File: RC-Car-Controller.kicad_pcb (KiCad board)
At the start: 2 copper layers, 72 parts, among them J1 USB_C_Receptacle_USB2.0, J2 Power_Input, J3 Screw_Terminal_01x02, J4 Motor_1_input, J5 Motor_2_input, SW1 SW_Push, SW2 SW_Push, U1 W25Q32JVSS, U2 ESP32-C3, U3 USBLC6-2SC6, U4 LMR14020SDDAR, U6 BMI055, U7 SPX3819M5-L-3-3, U8 DRV8874PWPR, U9 DRV8874PWPR, X1 40MHz

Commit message: Update placement
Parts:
- removed J3: Screw_Terminal_01x02, TerminalBlock:TerminalBlock_bornier-2_P5.08mm
- removed R11, R5, R6: 5k1, Resistor_SMD:R_0603_1608Metric
- removed R7: 1k, Resistor_SMD:R_0603_1608Metric
- removed R9: 10K, Resistor_SMD:R_0603_1608Metric
- removed SW1: SW_Push, Button_Switch_SMD:SW_Push_SPST_NO_Alps_SKRK
- removed X1: 40MHz, Crystal:Crystal_SMD_2520-4Pin_2.5x2.0mm
- added C34: 1uF, Capacitor_SMD:C_0402_1005Metric, F.Cu at (62.9, 35.9)
- added C35: 100n, Capacitor_SMD:C_0402_1005Metric, F.Cu at (37.4, 81.8)
- added C36: 22n, Capacitor_SMD:C_0402_1005Metric, F.Cu at (70.1, 51.9)
- added C37: 100n, Capacitor_SMD:C_0402_1005Metric, F.Cu at (71.9, 51.9)
- added C38: 100n, Capacitor_SMD:C_0402_1005Metric, F.Cu at (72.9, 50.8)
- added C39: 100u, Capacitor_SMD:C_0805_2012Metric, F.Cu at (73.6, 49.3)
- added C40: 100n, Capacitor_SMD:C_0402_1005Metric, F.Cu at (71.9, 68.9)
- added C41: 22n, Capacitor_SMD:C_0402_1005Metric, F.Cu at (69.9, 68.9)
- added C42: 100n, Capacitor_SMD:C_0402_1005Metric, F.Cu at (73.0, 67.9)
- added C43: 100u, Capacitor_SMD:C_0805_2012Metric, F.Cu at (73.7, 66.4)
- added C44: 100u, Capacitor_SMD:C_0805_2012Metric, F.Cu at (36.6, 83.3)
- added J6: MOTOR_3_OUTPUT, TerminalBlock:TerminalBlock_bornier-2_P5.08mm, F.Cu at (27.4, 54.9)
- added J7: MOTOR_4_OUTPUT, TerminalBlock:TerminalBlock_bornier-2_P5.08mm, F.Cu at (27.4, 71.4)
- added R14: 10K, Resistor_SMD:R_0603_1608Metric, F.Cu at (56.1, 68.9)
- added R15: 10K, Resistor_SMD:R_0603_1608Metric, F.Cu at (56.1, 65.7)
- added SW4: SW_Push, Button_Switch_SMD:SW_Push_SPST_NO_Alps_SKRK, F.Cu at (60.2, 81.6)
- added U10: DRV8874PWPR, Libraries:SOP65P640X120-17N, F.Cu at (71.5, 74.3)
- added U11: DRV8874PWPR, Libraries:SOP65P640X120-17N, F.Cu at (38.8, 74.7)
- added X2: 40MHz, KiCADv7:OSC_X322516MLB4SI, F.Cu at (66.2, 39.1)
- C1: value 100n -> 4.7u/100v; footprint Capacitor_SMD:C_0603_1608Metric -> Capacitor_SMD:C_1812_4532Metric
- C10, C9: value 10p -> 100n
- C11: value 100n -> 22n; footprint Capacitor_SMD:C_0603_1608Metric -> Capacitor_SMD:C_0402_1005Metric
- C12, C18, C20, C21, C22, C3, C30, C32, C4, C7: footprint Capacitor_SMD:C_0603_1608Metric -> Capacitor_SMD:C_0402_1005Metric
- C13, C24: value 10u -> 100n; footprint Capacitor_SMD:C_0603_1608Metric -> Capacitor_SMD:C_0402_1005Metric
- C14: value 4.7u/100v -> 100u; footprint Capacitor_SMD:C_1812_4532Metric -> Capacitor_SMD:C_0805_2012Metric
- C15: value 100n/100v -> 100n; footprint Capacitor_SMD:C_0805_2012Metric -> Capacitor_SMD:C_0402_1005Metric
- C16: value 0.1u -> 100n; footprint Capacitor_SMD:C_0603_1608Metric -> Capacitor_SMD:C_0402_1005Metric
- C17: value 10u -> 22n; footprint Capacitor_SMD:C_0603_1608Metric -> Capacitor_SMD:C_0402_1005Metric
- C19, C27, C6: value 100n -> 10u
- C2: value 10u -> 100n/100v; footprint Capacitor_SMD:C_1210_3225Metric -> Capacitor_SMD:C_0805_2012Metric
- C23: value 100n -> 20p; footprint Capacitor_SMD:C_0603_1608Metric -> Capacitor_SMD:C_0402_1005Metric
- C25: value 10u/50v -> 1u; footprint Capacitor_SMD:C_1210_3225Metric -> Capacitor_SMD:C_0402_1005Metric
- C26: value 22n -> 20p; footprint Capacitor_SMD:C_0603_1608Metric -> Capacitor_SMD:C_0402_1005Metric
- C28: value 100n -> 1u; footprint Capacitor_SMD:C_0603_1608Metric -> Capacitor_SMD:C_0402_1005Metric
- C29: value 100u -> 100n; footprint Capacitor_SMD:C_0603_1608Metric -> Capacitor_SMD:C_0402_1005Metric
- C31: value 22n -> 100n; footprint Capacitor_SMD:C_0603_1608Metric -> Capacitor_SMD:C_0402_1005Metric
- C33: value 100u -> 10nF; footprint Capacitor_SMD:C_0603_1608Metric -> Capacitor_SMD:C_0402_1005Metric
- C5: value 100n -> 10u/50v; footprint Capacitor_SMD:C_0603_1608Metric -> Capacitor_SMD:C_1210_3225Metric
- D2: value LED -> D_Schottky; footprint LED_SMD:LED_0603_1608Metric -> KiCADv6:DO-220AA_SS2PH10-M3&slash_84A_VIS
- D3: value D_Schottky -> LED; footprint KiCADv6:DO-220AA_SS2PH10-M3&slash_84A_VIS -> LED_SMD:LED_0603_1608Metric
- J4: value Motor_1_input -> MOTOR_1_OUTPUT
- J5: value Motor_2_input -> MOTOR_2_OUTPUT
- L1: value 2n2 -> 15uH/2.5A; footprint Inductor_SMD:L_0603_1608Metric -> Inductor_SMD:L_Bourns_SRN6045TA
- L3: value 15uH/2.5A -> 2n2; footprint Inductor_SMD:L_Bourns_SRN6045TA -> Inductor_SMD:L_0402_1005Metric
- R1: value 5k1 -> 1k
- R10: value 10K -> 5k1
- R2, R8: value 470R -> 5k1; footprint Resistor_SMD:R_0402_1005Metric -> Resistor_SMD:R_0603_1608Metric
- R3: value 22R -> 5k1; footprint Resistor_SMD:R_0402_1005Metric -> Resistor_SMD:R_0603_1608Metric
- U1: value W25Q32JVSS -> LMR14020SDDAR; footprint Package_SO:SOIC-8_5.23x5.23mm_P1.27mm -> Libraries:VREG_LM5017MR_NOPB
- U2: value ESP32-C3 -> SPX3819M5-L-3-3; footprint Package_DFN_QFN:QFN-32-1EP_5x5mm_P0.5mm_EP3.45x3.45mm -> Package_TO_SOT_SMD:SOT-23-5
- U4: value LMR14020SDDAR -> BMI055; footprint Libraries:VREG_LM5017MR_NOPB -> KiCADv6:LGA16_BMI055_BOS
- U5: value ~ -> DRV8874PWPR; footprint RF_Antenna:Texas_SWRA117D_2.4GHz_Right -> Libraries:SOP65P640X120-17N
- U6: value BMI055 -> W25Q32JVSS; footprint KiCADv6:LGA16_BMI055_BOS -> Package_SO:SOIC-8_5.23x5.23mm_P1.27mm
- U7: value SPX3819M5-L-3-3 -> ~; footprint Package_TO_SOT_SMD:SOT-23-5 -> RF_Antenna:Texas_SWRA117D_2.4GHz_Left
- U8: value DRV8874PWPR -> ESP32-S3; footprint Libraries:SOP65P640X120-17N -> Package_DFN_QFN:QFN-56-1EP_7x7mm_P0.4mm_EP5.6x5.6mm
- moved U4 139.2 mm to (42.6, 38.1)
- moved L3 133.3 mm to (58.9, 33.1), turned to 180 degrees
- moved R4 129.3 mm to (38.3, 38.9), turned to 180 degrees
- moved C18 113.3 mm to (38.4, 80.7), turned to 0 degrees
- moved R2 113.3 mm to (52.6, 111.4), turned to 90 degrees
- moved C31 113.1 mm to (51.7, 39.2), turned to -90 degrees
- moved C17 109.8 mm to (40.4, 80.7), turned to 180 degrees
- moved C30 109.8 mm to (59.9, 34.1)
- moved C33 107.0 mm to (62.9, 36.9)
- moved C11 105.8 mm to (41.1, 62.3), turned to 180 degrees
- moved C32 105.5 mm to (62.9, 40.2), turned to 90 degrees
- moved R8 100.4 mm to (51.8, 76.2)
- moved C13 96.0 mm to (38.3, 63.3), turned to 180 degrees
- moved C12 95.2 mm to (39.4, 62.3)
- moved C9 94.5 mm to (39.4, 37.1), turned to 90 degrees
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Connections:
- C1 pad 1: /INT_GYR_GPIO9 -> +36V
- C10 pad 1: Net-(U2-XTAL_N) -> +3V3
- C11 pad 1: /CHIP_EN -> Net-(U5-CPL)
- C11 pad 2: GND -> Net-(U5-CPH)
- C12 pad 1: /VDD_SPI -> +36V
- C12 pad 2: GND -> Net-(U5-VCP)
- C13 pad 1: /VDD_SPI -> +36V
- C15 pad 1: +36V -> /ESP32-S3 Microcontroller /CHIP_EN
- C16 pad 1: Net-(U4-SS) -> /ESP32-S3 Microcontroller /CHIP_BOOT
- C17 pad 1: +5V -> Net-(U11-CPL)
- C17 pad 2: GND -> Net-(U11-CPH)
- C18 pad 1: Net-(U7-BP) -> +36V
- C18 pad 2: GND -> Net-(U11-VCP)
- C19 pad 1: +3V3 -> /ESP32-S3 Microcontroller /VDD_SPI
- C2 pad 1: +3V3 -> +36V
- C20 pad 1: +3V3 -> /ESP32-S3 Microcontroller /VDD_SPI
- C21 pad 1: /RF -> /ESP32-S3 Microcontroller /RF
- C23 pad 1: Net-(U4-BOOT) -> Net-(U8-XTAL_N)
- C23 pad 2: Net-(D1-K) -> GND
- C24 pad 1: +3V3 -> /ESP32-S3 Microcontroller /VDD_SPI
- C25 pad 1: Net-(D3-A) -> /ESP32-S3 Microcontroller /VDD_SPI
- C26 pad 1: Net-(U8-CPL) -> Net-(U8-XTAL_P)
- C26 pad 2: Net-(U8-CPH) -> GND
- C27 pad 1: +36V -> +3V3
- C27 pad 2: Net-(U8-VCP) -> GND
- C28 pad 1: +36V -> +3V3
- C29 pad 1: +36V -> +3V3
- C3 pad 1: +3V3 -> Net-(U1-SS)
- C30 pad 1: +36V -> /ESP32-S3 Microcontroller /V_RF
- C30 pad 2: Net-(U9-VCP) -> GND
- C31 pad 1: Net-(U9-CPL) -> +3V3
- C31 pad 2: Net-(U9-CPH) -> GND
- C32 pad 1: +36V -> +3V3
- C33 pad 1: +36V -> +3V3
- C4 pad 1: +3V3 -> Net-(U1-BOOT)
- C4 pad 2: GND -> Net-(D1-K)
- C5 pad 1: +3V3 -> Net-(D2-A)
- C6 pad 1: /V_RF -> +5V
- C7 pad 1: +3V3 -> Net-(U2-BP)
- C9 pad 1: Net-(C9-Pad1) -> +3V3
- D2 pad 1: Net-(D2-K) -> +5V
- D2 pad 2: +3V3 -> Net-(D2-A)
- D3 pad 1: +5V -> Net-(D3-K)
- D3 pad 2: Net-(D3-A) -> +3V3
- J4 pad 1: /Connectors/MOTOR_1_OUT_2 -> MOTOR_1_OUT_1
- J4 pad 2: /Connectors/MOTOR_1_OUT_1 -> MOTOR_1_OUT_2
- J5 pad 1: /Connectors/MOTOR_2_OUT_2 -> MOTOR_2_OUT_1
- J5 pad 2: /Connectors/MOTOR_2_OUT_1 -> MOTOR_2_OUT_2
- L1 pad 1: /RF -> Net-(D1-K)
- L1 pad 2: Net-(C22-Pad1) -> Net-(D2-A)
- L2 pad 1: /V_RF -> /ESP32-S3 Microcontroller /RF
- L2 pad 2: +3V3 -> Net-(C22-Pad1)
- L3 pad 1: Net-(D1-K) -> /ESP32-S3 Microcontroller /V_RF
- L3 pad 2: Net-(D3-A) -> +3V3
- R1 pad 1: +3V3 -> Net-(D3-K)
- R1 pad 2: /INT_GYR_GPIO9 -> GND
- R10 pad 1: /MOTOR_VREF -> +3V3
- R10 pad 2: GND -> /ESP32-S3 Microcontroller /CHIP_BOOT
- R12 pad 1: /FSPI_NCS2 -> /ESP32-S3 Microcontroller /SPID
- R2 pad 1: Net-(U2-U0TXD/GPIO21) -> Net-(J1-CC2)
- R2 pad 2: /GPIO_21_TX -> GND
- R3 pad 1: Net-(C9-Pad1) -> Net-(J1-CC1)
- R3 pad 2: Net-(U2-XTAL_P) -> GND
- R4 pad 1: +3V3 -> FSPI_NCS2
- R4 pad 2: /CHIP_EN -> +3V3
- R8 pad 1: /GPIO_20_RX -> +3V3
- R8 pad 2: Net-(U2-U0RXD/GPIO20) -> /ESP32-S3 Microcontroller /CHIP_EN
- R_FBT1 pad 1: Net-(D3-A) -> Net-(D2-A)
- R_T1 pad 1: Net-(U4-RT/SYNC) -> Net-(U1-RT/SYNC)
- SW2 pad 2: /INT_GYR_GPIO9 -> /ESP32-S3 Microcontroller /CHIP_EN
- U1 pad 1: /SPICSO -> Net-(U1-BOOT)
- U1 pad 2: /SPIQ -> +36V
- U1 pad 3: /SPIWP -> +36V
- U1 pad 4: GND -> Net-(U1-RT/SYNC)
- U1 pad 5: /SPID -> /Power/B_FB
- U1 pad 6: /SPICLK -> Net-(U1-SS)
- U1 pad 7: /SPIHD -> GND
- U1 pad 8: /VDD_SPI -> Net-(D1-K)
- U2 pad 1: /RF -> +5V
- U2 pad 2: /V_RF -> GND
- U2 pad 3: /V_RF -> +5V
- U2 pad 4: /MOTOR_2_DIRECTION -> Net-(U2-BP)
- U2 pad 5: /MOTOR_1_DIRECTION -> +3V3
- U4 pad 1: Net-(U4-BOOT) -> unconnected-(U4-Pad1)
- U4 pad 10: (no net) -> FSPI_Q
- U4 pad 11: (no net) -> +3V3
- U4 pad 12: (no net) -> INT_GYR_GPIO9
- U4 pad 13: (no net) -> unconnected-(U4-Pad13)
- U4 pad 14: (no net) -> FSPI_NCS
- U4 pad 15: (no net) -> FSPI_Q
- U4 pad 16: (no net) -> INT_ACC
- U4 pad 2: +36V -> GND
- U4 pad 3: +36V -> +3V3
- U4 pad 4: Net-(U4-RT/SYNC) -> GND
- U4 pad 5: /Power/B_FB -> FSPI_NCS2
- U4 pad 6: Net-(U4-SS) -> GND
- U4 pad 8: Net-(D1-K) -> FSPI_CLK
- U4 pad 9: GND -> FSPI_D
- U5 pad 1: Net-(C22-Pad1) -> MOTOR_3_PWM
- U5 pad 2: GND -> MOTOR_3_DIRECTION
- U6 pad 1: unconnected-(U6-Pad1) -> /ESP32-S3 Microcontroller /SPICSO
- U6 pad 2: GND -> /ESP32-S3 Microcontroller /SPIQ
- U6 pad 3: +3V3 -> /ESP32-S3 Microcontroller /SPIWP
- U6 pad 5: /Sensors/FSPI_NCS2 -> /ESP32-S3 Microcontroller /SPID
- U6 pad 6: GND -> /ESP32-S3 Microcontroller /SPICLK
- U6 pad 7: GND -> /ESP32-S3 Microcontroller /SPIHD
- U6 pad 8: /Sensors/FSPI_CLK -> /ESP32-S3 Microcontroller /VDD_SPI
- U7 pad 1: +5V -> Net-(C22-Pad1)
- U8 pad 1: /MOTOR_1_PWM -> /ESP32-S3 Microcontroller /RF
- U8 pad 10: /MOTOR_1_OUT_2 -> MOTOR_3_PWM
- U8 pad 11: +36V -> MOTOR_3_DIRECTION
- U8 pad 12: Net-(U8-VCP) -> MOTOR_4_PWM
- U8 pad 13: Net-(U8-CPH) -> MOTOR_4_DIRECTION
- U8 pad 14: Net-(U8-CPL) -> unconnected-(U8-GPIO9/ADC1_CH8-Pad14)
- U8 pad 15: GND -> unconnected-(U8-GPIO10/ADC1_CH9-Pad15)
- U8 pad 16: GND -> INT_GYR_GPIO9
- U8 pad 17: (no net) -> INT_ACC
- U8 pad 2: /MOTOR_1_DIRECTION -> /ESP32-S3 Microcontroller /V_RF
- U8 pad 3: +3V3 -> /ESP32-S3 Microcontroller /V_RF
- U8 pad 4: unconnected-(U8-NFAULT-Pad4) -> /ESP32-S3 Microcontroller /CHIP_EN
- U8 pad 5: /MOTOR_VREF -> /ESP32-S3 Microcontroller /CHIP_BOOT
- U8 pad 6: unconnected-(U8-IPROPI-Pad6) -> MOTOR_1_PWM
- U8 pad 7: GND -> MOTOR_1_DIRECTION
- U8 pad 8: /MOTOR_1_OUT_1 -> MOTOR_2_PWM
- U8 pad 9: GND -> MOTOR_2_DIRECTION
- U9 pad 1: /MOTOR_2_PWM -> MOTOR_2_PWM
- U9 pad 10: /MOTOR_2_OUT_2 -> MOTOR_2_OUT_2
- U9 pad 2: /MOTOR_2_DIRECTION -> MOTOR_2_DIRECTION
- U9 pad 5: /MOTOR_VREF -> /Motors/MOTOR_VREF
- U9 pad 8: /MOTOR_2_OUT_1 -> MOTOR_2_OUT_1
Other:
- copper layers 2 -> 4

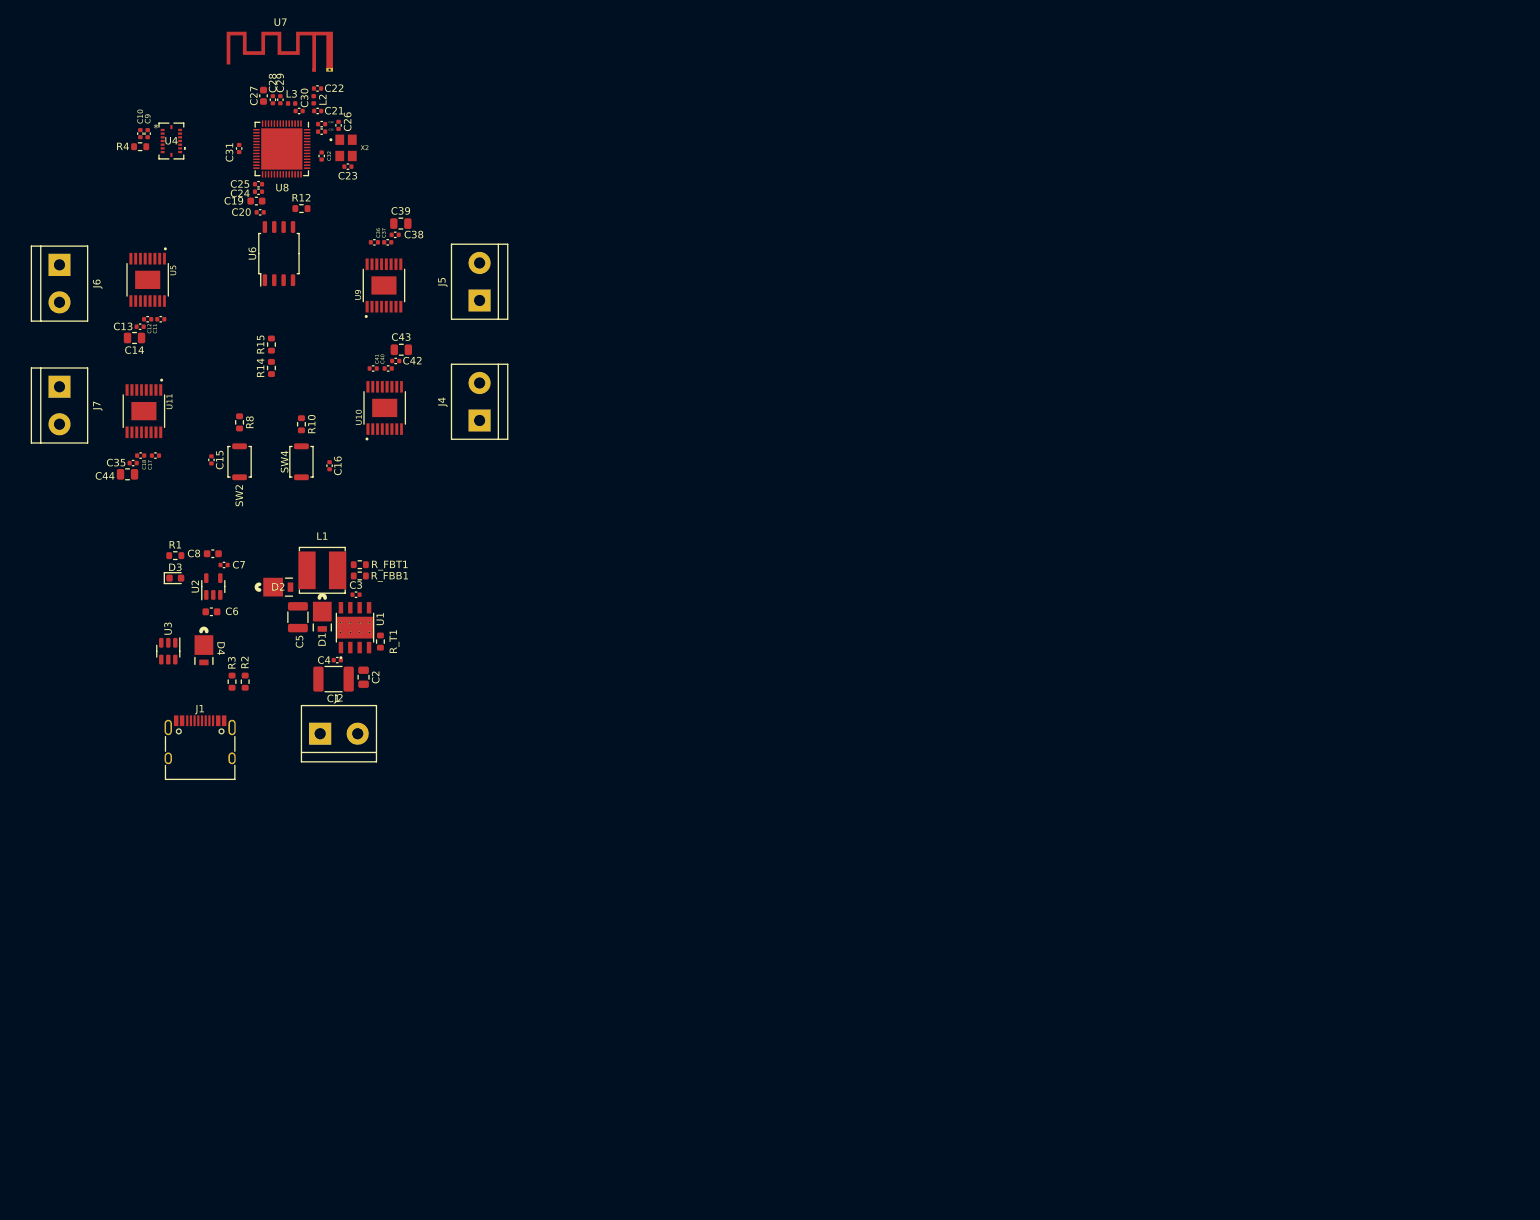
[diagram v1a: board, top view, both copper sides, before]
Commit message: route usb and flash
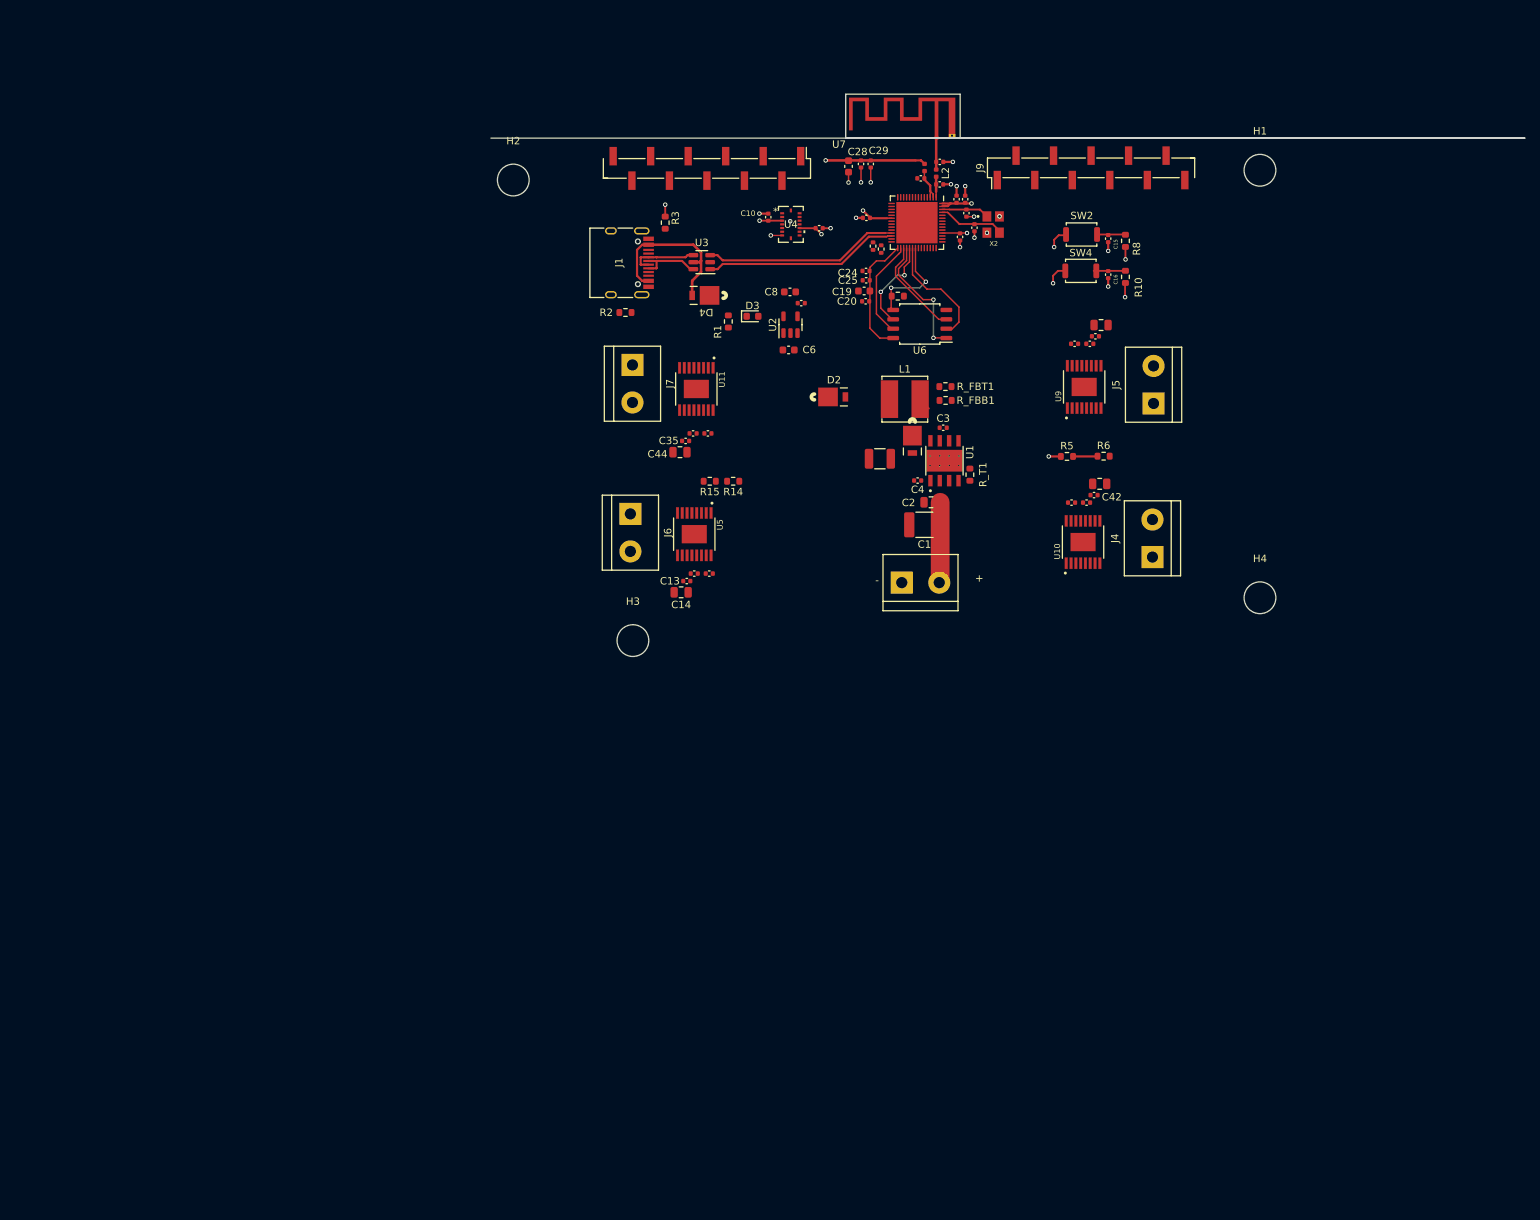
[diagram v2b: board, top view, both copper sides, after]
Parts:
- added H1: MountingHole, MountingHole:MountingHole_4.3mm_M4, F.Cu at (190.0, 42.1)
- added H2: MountingHole, MountingHole:MountingHole_4.3mm_M4, F.Cu at (88.9, 43.4)
- added H3: MountingHole, MountingHole:MountingHole_4.3mm_M4, F.Cu at (105.1, 105.8)
- added H4: MountingHole, MountingHole:MountingHole_4.3mm_M4, F.Cu at (190.0, 100.0)
- added J3: Conn_01x11_Socket, Connector_PinHeader_2.54mm:PinHeader_1x11_P2.54mm_Vertical_SMD_Pin1Left, F.Cu at (115.1, 41.9)
- added J9: Conn_01x11_Socket, Connector_PinHeader_2.54mm:PinHeader_1x11_P2.54mm_Vertical_SMD_Pin1Left, F.Cu at (167.1, 41.8)
- added R5: 10K, Resistor_SMD:R_0603_1608Metric, F.Cu at (163.9, 80.9)
- added R6: 10K, Resistor_SMD:R_0603_1608Metric, F.Cu at (168.8, 80.8)
- added R7: 1k, Resistor_SMD:R_0402_1005Metric, F.Cu at (137.6, 52.4)
- R4: value 5k1 -> 1k; footprint Resistor_SMD:R_0603_1608Metric -> Resistor_SMD:R_0402_1005Metric
- moved C15 125.1 mm to (169.4, 51.4)
- moved R8 122.5 mm to (171.8, 51.7), turned to 90 degrees
- moved SW2 118.1 mm to (165.8, 50.8), turned to 0 degrees
- moved R10 113.4 mm to (171.8, 56.5), turned to 90 degrees
- moved SW4 108.7 mm to (165.7, 55.7), turned to 0 degrees
- moved C16 108.6 mm to (169.4, 56.2)
- moved R4 101.3 mm to (138.7, 52.8), turned to 90 degrees
- moved U10 96.3 mm to (166.0, 92.5)
- moved C40 96.3 mm to (166.5, 87.1)
- moved C41 96.3 mm to (164.5, 87.1)
- moved C42 96.3 mm to (167.5, 86.1)
- moved C43 96.3 mm to (168.3, 84.6)
- moved C37 96.1 mm to (167.0, 65.6)
- moved U9 95.8 mm to (166.2, 71.4)
- moved C36 95.8 mm to (164.9, 65.6)
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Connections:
- net /ESP32-S3 Microcontroller /CHIP_EN renamed /ESP32-S3 Microcontroller /RESET
- net Net-(C22-Pad1) renamed /ESP32-S3 Microcontroller /RF_FEED
- net Net-(D1-K) renamed /Power/SW
- net Net-(D2-A) renamed /Power/SMP_OUT
- net Net-(U1-BOOT) renamed /Power/SMP_BOOT
- net Net-(U1-RT/SYNC) renamed /Power/SYNC
- net Net-(U1-SS) renamed /Power/SS
- J2 pad 1: +36V -> GND
- J2 pad 2: GND -> +36V
- R4 pad 1: FSPI_NCS2 -> +3V3
- R4 pad 2: +3V3 -> SCL
- U4 pad 10: FSPI_Q -> ADDR_ACCEL
- U4 pad 12: INT_GYR_GPIO9 -> INT_GYR_1
- U4 pad 14: FSPI_NCS -> unconnected-(U4-Pad14)
- U4 pad 15: FSPI_Q -> ADDR_GYRO
- U4 pad 16: INT_ACC -> INT_ACC_1
- U4 pad 5: FSPI_NCS2 -> unconnected-(U4-Pad5)
- U4 pad 7: GND -> +3V3
- U4 pad 8: FSPI_CLK -> SCL
- U4 pad 9: FSPI_D -> SDA
- U8 pad 10: MOTOR_3_PWM -> GPIO5
- U8 pad 11: MOTOR_3_DIRECTION -> GPIO6
- U8 pad 12: MOTOR_4_PWM -> GPIO7
- U8 pad 13: MOTOR_4_DIRECTION -> GPIO8
- U8 pad 14: unconnected-(U8-GPIO9/ADC1_CH8-Pad14) -> GPIO9
- U8 pad 15: unconnected-(U8-GPIO10/ADC1_CH9-Pad15) -> GPIO10
- U8 pad 16: INT_GYR_GPIO9 -> GPIO11
- U8 pad 17: INT_ACC -> GPIO12
- U8 pad 18: FSPI_Q -> GPIO13
- U8 pad 19: FSPI_NCS2 -> GPIO14
- U8 pad 21: unconnected-(U8-GPIO15/ADC2_CH4/XTAL_32K_P-Pad21) -> GPIO15
- U8 pad 22: unconnected-(U8-GPIO16/ADC2_CH5/XTAL_32K_N-Pad22) -> GPIO16
- U8 pad 23: FSPI_NCS -> INT_GYR_1
- U8 pad 24: unconnected-(U8-GPIO18/ADC2_CH7-Pad24) -> INT_ACC_1
- U8 pad 27: unconnected-(U8-GPIO21-Pad27) -> SDA
- U8 pad 28: unconnected-(U8-SPI_CS1/GPIO26-Pad28) -> SCL
- U8 pad 36: unconnected-(U8-SPICLK_N/GPIO48-Pad36) -> MOTOR_4_DIRECTION
- U8 pad 37: unconnected-(U8-SPICLK_P/GPIO47-Pad37) -> MOTOR_4_PWM
- U8 pad 38: unconnected-(U8-GPIO33-Pad38) -> MOTOR_3_DIRECTION
- U8 pad 39: unconnected-(U8-GPIO34-Pad39) -> MOTOR_3_PWM
- U8 pad 40: unconnected-(U8-GPIO35-Pad40) -> MOTOR_2_DIRECTION
- U8 pad 41: unconnected-(U8-GPIO36-Pad41) -> MOTOR_2_PWM
- U8 pad 42: unconnected-(U8-GPIO37-Pad42) -> MOTOR_1_DIRECTION
- U8 pad 43: unconnected-(U8-GPIO38-Pad43) -> MOTOR_1_PWM
- U8 pad 44: FSPI_CLK -> GPIO39
- U8 pad 45: FSPI_D -> GPIO40
- U8 pad 47: unconnected-(U8-MTDI/JTAG/GPIO41-Pad47) -> GPIO41
- U8 pad 48: unconnected-(U8-MTMS/JTAG/GPIO42-Pad48) -> GPIO42
- U8 pad 49: unconnected-(U8-U0TXD/PROG/GPIO43-Pad49) -> GPIO43_TX
- U8 pad 50: unconnected-(U8-U0RXD/PROG/GPIO44-Pad50) -> GPIO44_RX
- U8 pad 51: unconnected-(U8-GPIO45-Pad51) -> ADDR_GYRO
- U8 pad 52: unconnected-(U8-GPIO46-Pad52) -> ADDR_ACCEL
- U8 pad 6: MOTOR_1_PWM -> GPIO1
- U8 pad 7: MOTOR_1_DIRECTION -> GPIO2
- U8 pad 8: MOTOR_2_PWM -> GPIO3
- U8 pad 9: MOTOR_2_DIRECTION -> GPIO4
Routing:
- net +3V3: track 0.00 -> 39.7 mm, vias 0 -> 10
- net USB_D_P: track 0.00 -> 26.4 mm
- net USB_D_N: track 0.00 -> 26.4 mm
- net GND: track 0.00 -> 25.8 mm, vias 0 -> 21
- net +VBUS: track 0.00 -> 22.2 mm
- net /ESP32-S3 Microcontroller /SPICSO: track 0.00 -> 17.1 mm, vias 0 -> 2
- net /ESP32-S3 Microcontroller /VDD_SPI: track 0.00 -> 16.8 mm
- net /ESP32-S3 Microcontroller /SPIQ: track 0.00 -> 15.8 mm
- net /ESP32-S3 Microcontroller /SPIWP: track 0.00 -> 13.6 mm
- net /ESP32-S3 Microcontroller /SPIHD: track 0.00 -> 13.4 mm
- net /ESP32-S3 Microcontroller /SPID: track 0.00 -> 13.3 mm, vias 0 -> 2
- net /ESP32-S3 Microcontroller /SPICLK: track 0.00 -> 12.6 mm, vias 0 -> 2
- net +36V: track 0.00 -> 10.9 mm
- net /Connectors/C_D-: track 0.00 -> 9.32 mm
- net Net-(U8-XTAL_N): track 0.00 -> 9.02 mm
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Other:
- board outline added: 140 x 6 mm
- board text added: "+"
- board text added: "-"
